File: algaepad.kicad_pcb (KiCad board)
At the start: 2 copper layers, 10.6 x 5.5 mm, 64 parts, among them SW1 SW_Push, SW10 SW_Push, SW11 SW_Push, SW12 SW_Push, SW13 SW_Push, SW14 SW_Push, SW15 SW_Push, SW16 SW_Push, SW17 SW_Push, SW18 SW_Push, SW19 SW_Push, SW2 SW_Push, SW20 SW_Push, SW21 SW_Push, SW22 SW_Push, SW23 SW_Push, SW24 SW_Push, SW25 SW_Push, SW26 SW_Push, SW27 SW_Push, SW28 SW_Push, SW29 SW_Push, SW3 SW_Push, SW30 SW_Push, SW31 SW_Push, SW32 SW_Push, SW4 SW_Push, SW5 SW_Push, SW6 SW_Push, SW7 SW_Push, SW8 SW_Push, SW9 SW_Push

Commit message: start work in layout
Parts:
- moved SW32 145.5 mm to (182.7, 111.8)
- moved D1 144.8 mm to (40.1, 34.4), turned to -90 degrees
- moved D4 142.5 mm to (38.5, 98.2), turned to -90 degrees
- moved D7 131.3 mm to (61.3, 75.3), turned to -90 degrees
- moved D10 128.6 mm to (84.2, 55.0), turned to -90 degrees
- moved D9 126.7 mm to (84.2, 34.7), turned to -90 degrees
- moved D3 122.2 mm to (40.6, 77.9), turned to -90 degrees
- moved SW24 121.9 mm to (160.0, 50.6)
- moved D24 121.8 mm to (152.8, 55.0), turned to -90 degrees
- moved D23 119.8 mm to (152.4, 34.7), turned to -90 degrees
- moved D5 113.8 mm to (62.6, 35.6), turned to -90 degrees
- moved D8 111.4 mm to (61.0, 96.5), turned to -90 degrees
- moved D6 109.9 mm to (61.3, 55.0), turned to -90 degrees
- moved SW1 106.4 mm to (47.1, 29.4)
- moved D18 104.2 mm to (129.9, 34.7), turned to -90 degrees
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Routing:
- net ROW4: track 0.00 -> 139.9 mm
- net ROW3: track 0.00 -> 137.2 mm
- net ROW1: track 0.00 -> 136.5 mm
- net ROW2: track 0.00 -> 135.0 mm
- net COL7: track 0.00 -> 58.6 mm
- net COL6: track 0.00 -> 58.5 mm
- net COL4: track 0.00 -> 58.5 mm
- net COL5: track 0.00 -> 58.5 mm
- net ROW5: track 0.00 -> 46.5 mm
- net COL1: track 0.00 -> 45.3 mm
- net COL3: track 0.00 -> 44.8 mm
- net COL2: track 0.00 -> 44.3 mm
- net Net-(D3-Pad1): track 0.00 -> 5.73 mm
- net Net-(D1-Pad1): track 0.00 -> 3.93 mm
- net Net-(D5-Pad1): track 0.00 -> 3.93 mm
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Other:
- board size 10.6 x 5.5 mm -> 165.1 x 109.2 mm
- rule pad_to_mask_clearance: 0 -> 0.05

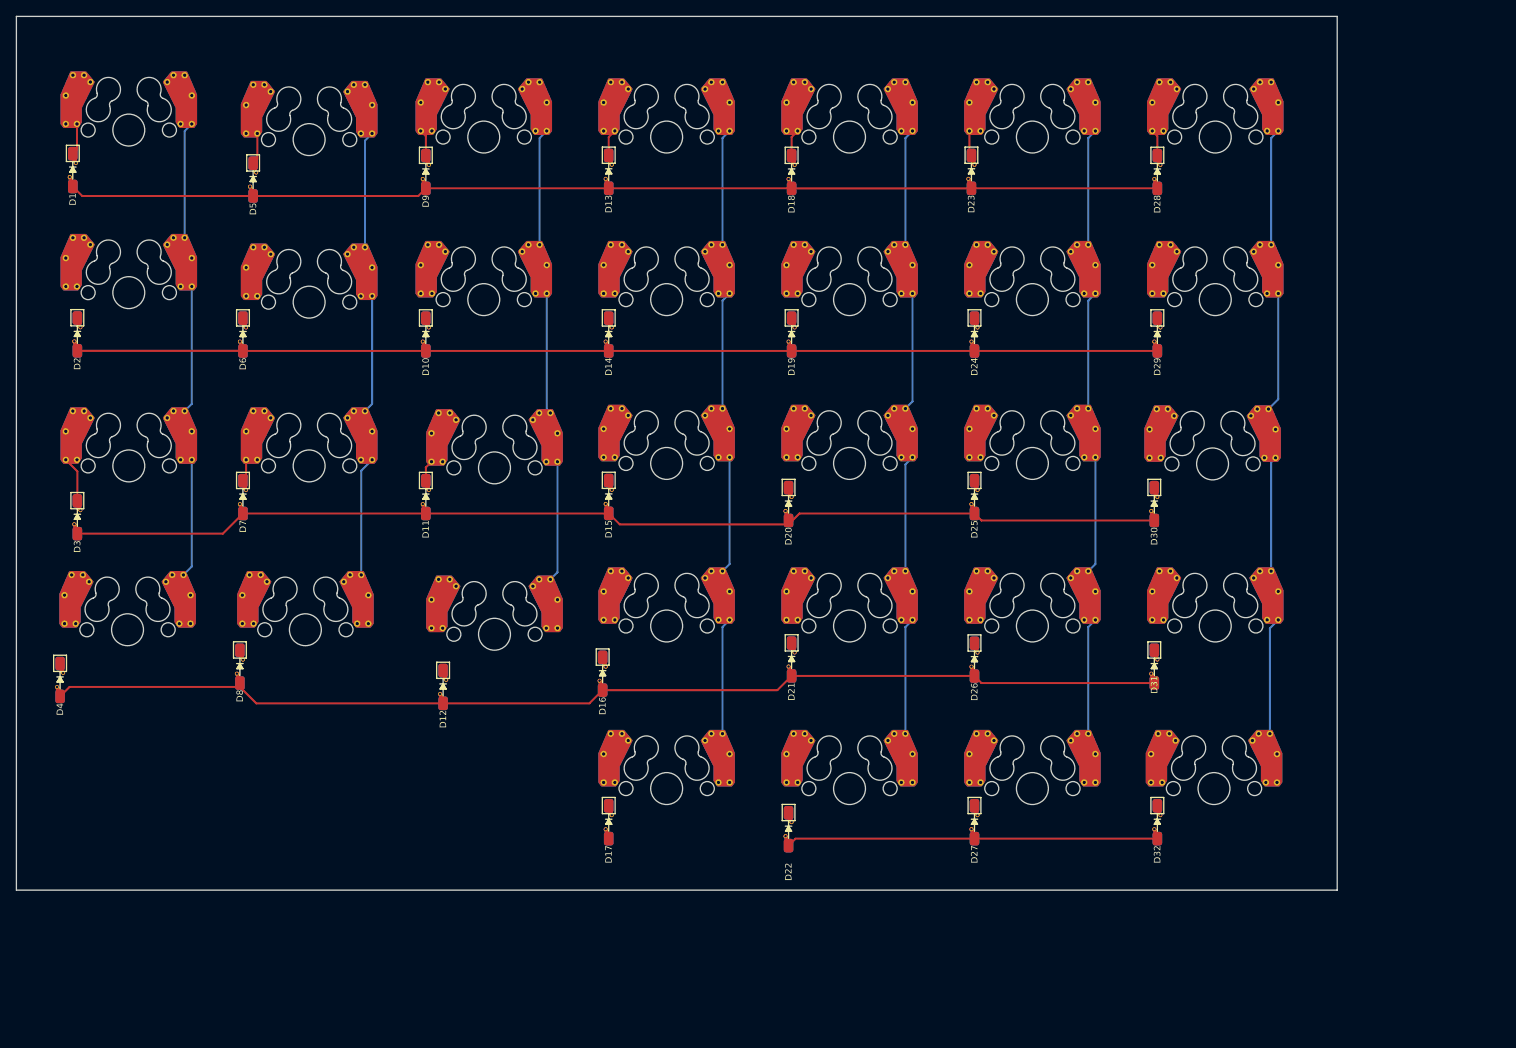
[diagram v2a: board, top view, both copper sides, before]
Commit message: first attempt at complete pcb layout
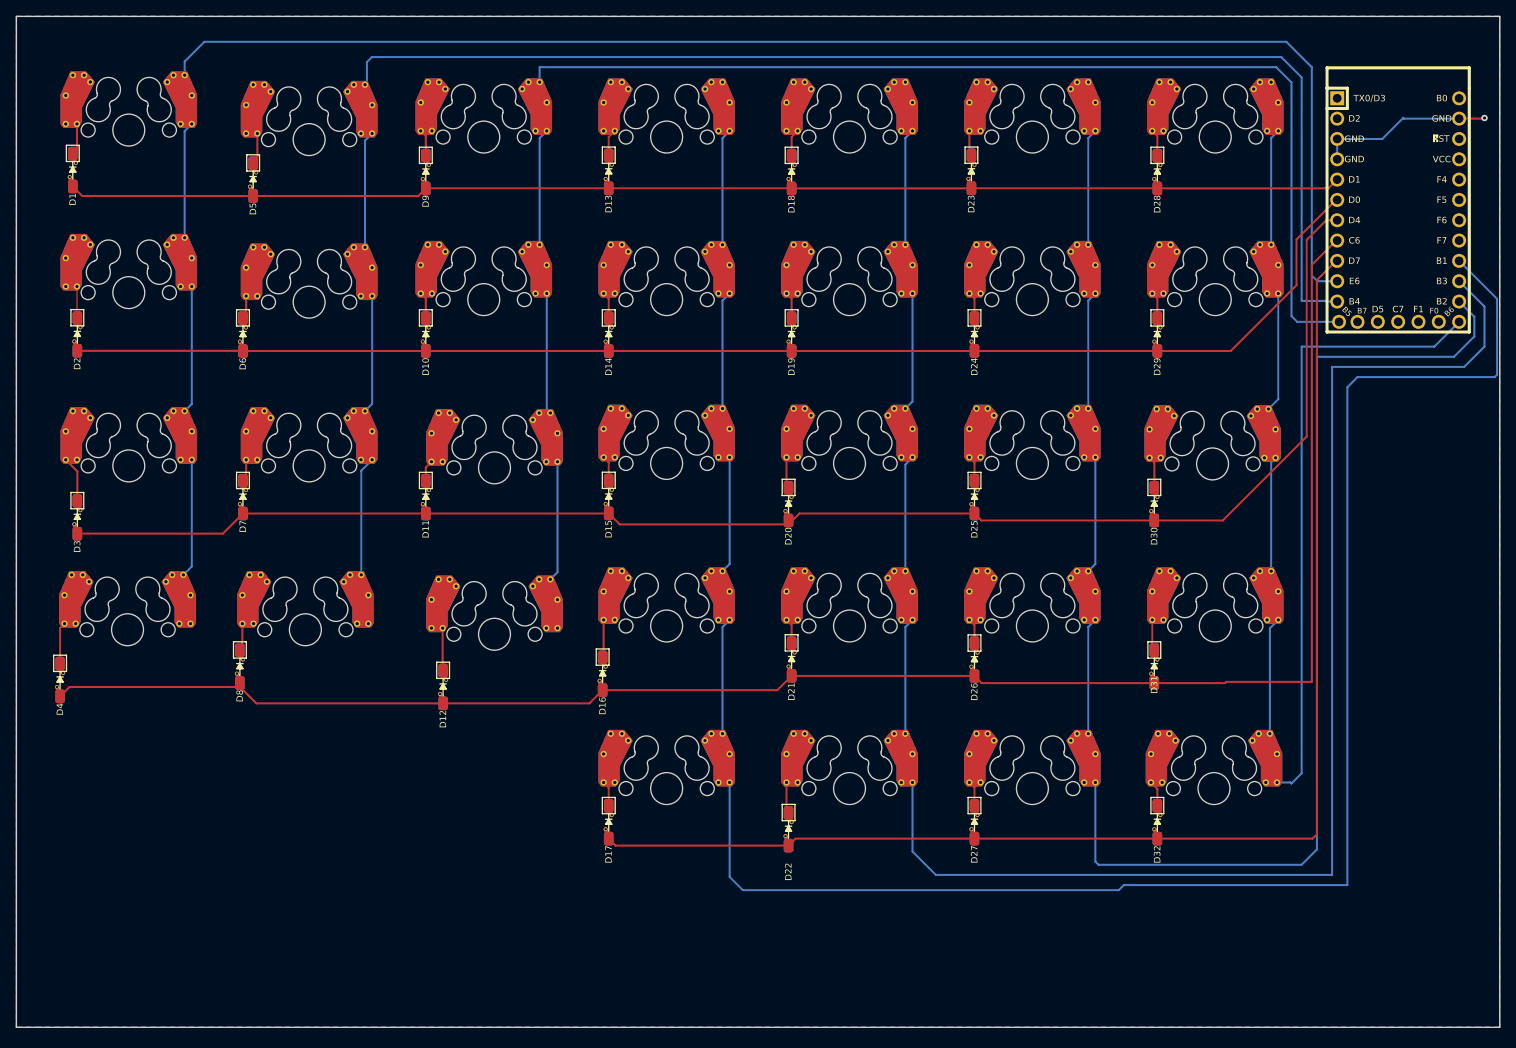
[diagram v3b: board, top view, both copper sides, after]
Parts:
- added U1: Elite-C, keebio-parts:Elite-C, F.Cu at (205.7, 39.5)
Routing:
- net COL4: track 58.5 -> 246.3 mm
- net COL1: track 45.3 -> 219.8 mm
- net COL5: track 58.5 -> 213.9 mm
- net COL2: track 44.3 -> 197.8 mm
- net COL3: track 44.8 -> 176.9 mm
- net COL6: track 58.5 -> 184.6 mm
- net ROW5: track 46.5 -> 162.1 mm
- net COL7: track 58.6 -> 136.6 mm
- net ROW4: track 139.9 -> 216.1 mm
- net ROW3: track 137.2 -> 189.8 mm
- net ROW2: track 135.0 -> 168.5 mm
- net ROW1: track 136.5 -> 159.4 mm
- net GND: track 0.00 -> 22.1 mm, vias 0 -> 1
- net Net-(D12-K): track 0.00 -> 5.32 mm
- net Net-(D4-K): track 0.00 -> 5.22 mm
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- added copper zone on B.Cu, net GND
- added copper zone on F.Cu, net GND
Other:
- board size 165.1 x 109.2 mm -> 185.4 x 126.4 mm
- rule pad_to_mask_clearance: 0.05 -> 0

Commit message: switch to SMT diode
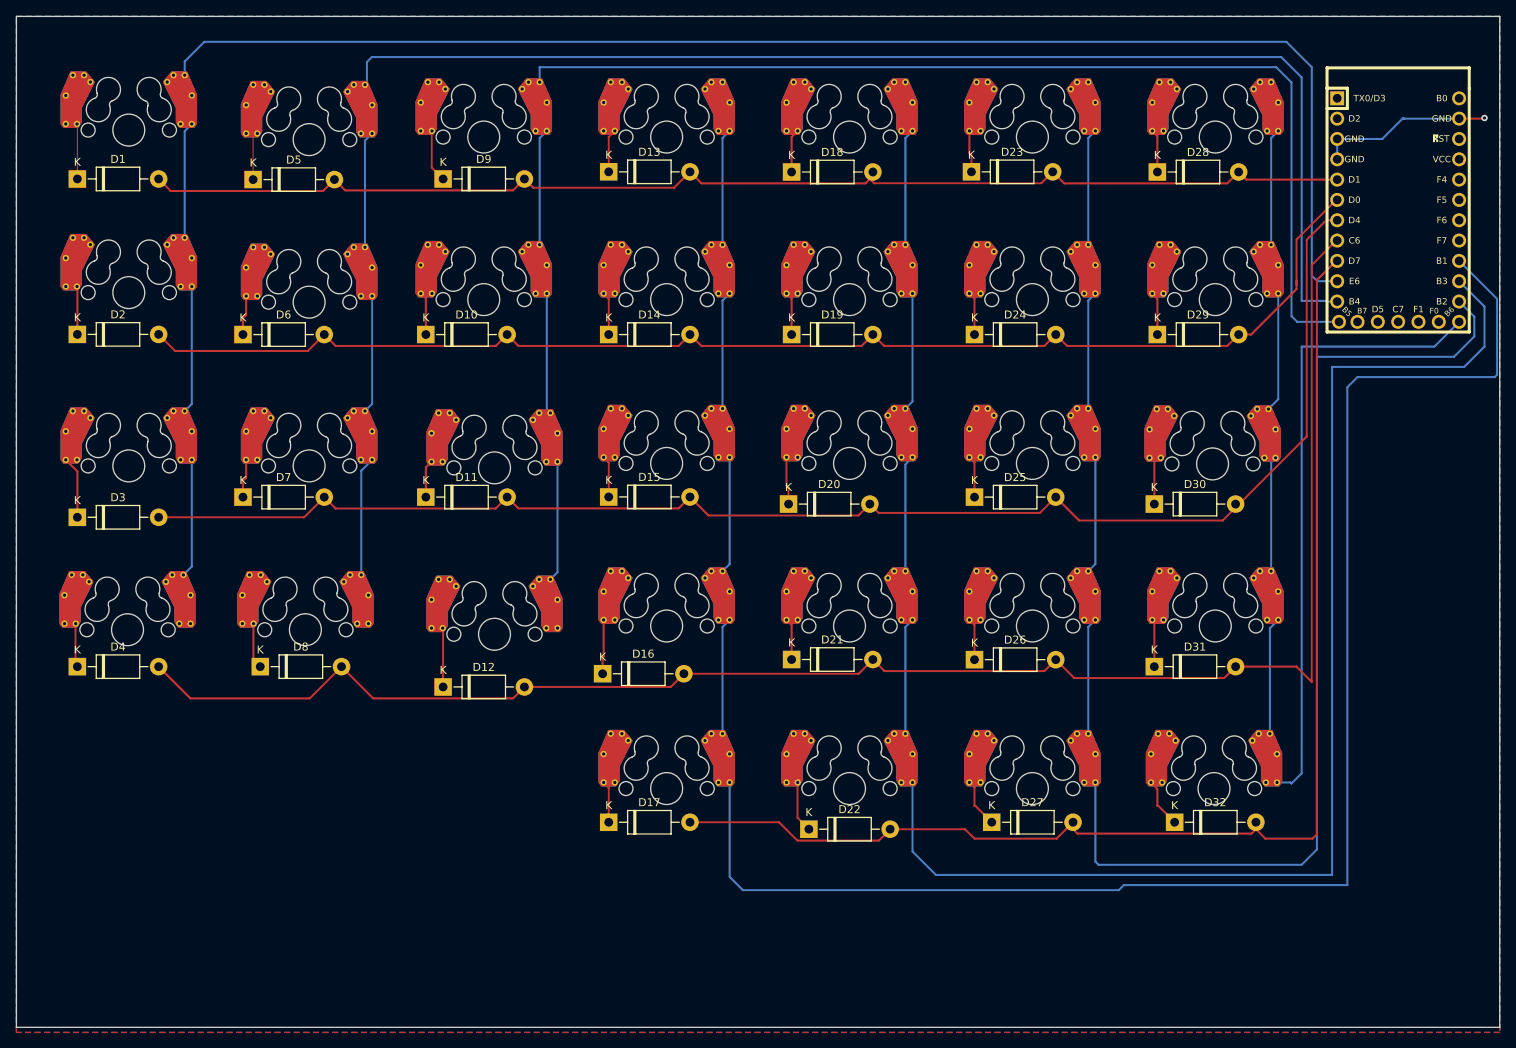
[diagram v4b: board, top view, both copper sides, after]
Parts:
- D1, D10, D11, D12, D13, D14, D15, D16, D17, D18, D19, D2, D20, D21, D22, D23, D24, D25, D26, D27, D28, D29, D3, D30, D31, D32, D4, D5, D6, D7, D8, D9: value 1N4148 -> 1N47xxA; footprint reversible-footprints:D_SOD-123 -> Diode_THT:D_DO-41_SOD81_P10.16mm_Horizontal
- moved D4 2.73 mm to (40.6, 96.5), turned to 0 degrees
- moved D22 2.54 mm to (132.1, 116.8), turned to 0 degrees
- moved D8 2.54 mm to (63.5, 96.5), turned to 0 degrees
- moved D9 2.33 mm to (86.4, 35.6), turned to 0 degrees
- moved D32 2.16 mm to (177.8, 116.0), turned to 0 degrees
- moved D27 2.16 mm to (154.9, 116.0), turned to 0 degrees
- moved D1 1.25 mm to (40.6, 35.6), turned to 0 degrees
- turned D10 to 0 degrees
- turned D11 to 0 degrees
- turned D12 to 0 degrees
- turned D13 to 0 degrees
- turned D14 to 0 degrees
- turned D15 to 0 degrees
- turned D16 to 0 degrees
- turned D17 to 0 degrees
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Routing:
- net Net-(D9-K): track 3.34 -> 10.9 mm
- net Net-(D1-K): track 3.93 -> 11.2 mm
- net ROW5: track 162.1 -> 155.1 mm
- net Net-(D22-K): track 3.90 -> 10.7 mm
- net Net-(D31-K): track 3.90 -> 10.6 mm
- net Net-(D8-K): track 3.45 -> 10.0 mm
- net Net-(D30-K): track 3.98 -> 10.4 mm
- net Net-(D2-K): track 3.95 -> 10.3 mm
- net Net-(D12-K): track 5.32 -> 11.7 mm
- net Net-(D5-K): track 3.93 -> 10.3 mm
- net ROW3: track 189.8 -> 184.6 mm
- net ROW4: track 216.1 -> 211.0 mm
- net ROW1: track 159.4 -> 154.3 mm
- net Net-(D4-K): track 5.22 -> 9.77 mm
- net Net-(D32-K): track 3.25 -> 6.26 mm
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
